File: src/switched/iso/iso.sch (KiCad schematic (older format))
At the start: 54 parts

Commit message: isolation stage rev 1
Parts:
- removed C?: 1n, symbol Device:C_Small
- removed C?: 33n, symbol Device:C_Small
- removed C? (x2): 2n2, symbol Device:C_Small
- removed C?: 47u, symbol Device:C
- removed C?: 100n, symbol Device:C_Small
- removed D? (x3): D, symbol Device:D
- removed IC?: NCP1252A, SOIC127P600X175-8N, symbol NCP1252CDR2G:NCP1252CDR2G
- removed Q?: Q_NMOS_DGS, symbol Device:Q_NMOS_DGS
- removed R?: 4, symbol Device:R_US
- removed R?: 5k571, symbol Device:R_US
- removed R?: 10R 2W, symbol Device:R_US
- removed R?: 24k, symbol Device:R_US
- removed R? (x2): 10k, symbol Device:R_US
- removed R?: 22k, symbol Device:R_US
- removed R?: 2k, symbol Device:R_US
- removed R?: 1k, symbol Device:R_US
- removed R?: 235, symbol Device:R_US
- removed R?: 565, symbol Device:R_US
- removed U?: TL431D, Package_SO:SOIC-8_3.9x4.9mm_P1.27mm, symbol Reference_Voltage:TL431D
- removed U?: OPAMP, symbol pspice:OPAMP
- added C1, C17, C18, C5, C7: 100n, Capacitor_SMD:C_0603_1608Metric_Pad1.08x0.95mm_HandSolder, symbol Device:C_Small
- added C10, C11, C12, C6, C9: 1n, Capacitor_SMD:C_0603_1608Metric_Pad1.08x0.95mm_HandSolder, symbol Device:C_Small
- added C15: 470n, Capacitor_SMD:C_0603_1608Metric_Pad1.08x0.95mm_HandSolder, symbol Device:C_Small
- added C2: 4.7u, Capacitor_THT:CP_Radial_D8.0mm_P3.50mm, symbol Device:C_Small
- added D1, D4, D5: 1N4007W, Diode_SMD:D_SOD-123F, symbol Device:D
- added IC1: NCP1252ADR2G, Package_SO:SOIC-8_3.9x4.9mm_P1.27mm, symbol NCP1252CDR2G:NCP1252CDR2G
- added Q2: TSD5N50MR, Package_TO_SOT_SMD:TO-252-2, symbol Device:Q_NMOS_GDS
- added R1: 1Meg, Resistor_SMD:R_1206_3216Metric_Pad1.30x1.75mm_HandSolder, symbol Device:R_US
- added R12: 10R, Resistor_THT:R_Axial_DIN0207_L6.3mm_D2.5mm_P2.54mm_Vertical, symbol Device:R_US
- added R15, R3: 1k, Resistor_THT:R_Axial_DIN0207_L6.3mm_D2.5mm_P2.54mm_Vertical, symbol Device:R_US
- added R16: 39k, Resistor_SMD:R_0603_1608Metric_Pad0.98x0.95mm_HandSolder, symbol Device:R_US
- added R18: 15k, Resistor_THT:R_Axial_DIN0309_L9.0mm_D3.2mm_P2.54mm_Vertical, symbol Device:R_US
- added R4, R5, R6, R7: 10, Resistor_SMD:R_0603_1608Metric_Pad0.98x0.95mm_HandSolder, symbol Device:R_US
- added RV1: 5k571, Potentiometer_SMD:Potentiometer_Bourns_TC33X_Vertical, symbol Device:R_POT_TRIM_US
- added RV2, RV3: 2.4, Potentiometer_SMD:Potentiometer_Bourns_TC33X_Vertical, symbol Device:R_POT_TRIM_US
- added RV4: 1k, Potentiometer_SMD:Potentiometer_Bourns_TC33X_Vertical, symbol Device:R_POT_TRIM_US
- added U1: NCP5106, Package_SO:SOIC-8_3.9x4.9mm_P1.27mm, symbol custom:NCP5106
- added U3: TL431LP, Package_TO_SOT_THT:TO-92_Inline, symbol Reference_Voltage:TL431LP
- added U4: MC34072, Package_SO:SOIC-8_3.9x4.9mm_P1.27mm, symbol custom:MC34072
- C13: renamed from C?; value 40u -> 330u; footprint (none) -> Capacitor_SMD:CP_Elec_10x14.3; Checked (none) -> yes; Link (none) -> https://lcsc.com/product-detail/New-Arrivals_Ymin-VKME1651J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; Working Voltage (none) -> 63
- C14, C19, C3, C8: renamed from C?; footprint (none) -> Capacitor_SMD:C_0603_1608Metric_Pad1.08x0.95mm_HandSolder; Checked (none) -> yes; Link (none) -> https://lcsc.com/product-detail/Multilayer-Ceramic-Capacito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; Notes (none) -> On PFC; Working Voltage (none) -> 50
- C16: renamed from C?; value 1u -> 470n; footprint (none) -> Capacitor_SMD:C_0603_1608Metric_Pad1.08x0.95mm_HandSolder; Checked (none) -> yes; Link (none) -> https://lcsc.com/product-detail/Multilayer-Ceramic-Capacito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; Notes (none) -> On PFC; Working Voltage (none) -> 25
- C4: renamed from C?; value 55n -> 47n; footprint (none) -> Capacitor_SMD:C_0603_1608Metric_Pad1.08x0.95mm_HandSolder; Checked (none) -> yes; Link (none) -> https://lcsc.com/product-detail/Multilayer-Ceramic-Capacito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; Working Voltage (none) -> 50
- D2, D3: renamed from D?; footprint (none) -> Diode_SMD:D_SOD-123; Checked (none) -> yes; Link (none) -> https://lcsc.com/product-detail/Zener-Diodes_Slkor-SLKORMIC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
- D6, D7: renamed from D?; footprint (none) -> Diode_SMD:D_SMC; Checked (none) -> yes; Link (none) -> https://lcsc.com/product-detail/Diodes-General-Purpose_Shan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
- D8: renamed from D?; footprint (none) -> Diode_SMD:D_SOD-123; Checked (none) -> yes; Link (none) -> https://lcsc.com/product-detail/Zener-Diodes_Shandong-Jingd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
- J1, J3: renamed from J?; footprint (none) -> Connector_Wire:SolderWire-1.5sqmm_1x02_P6mm_D1.7mm_OD3mm
- J2, J4: renamed from J?; footprint (none) -> Connector_PinSocket_2.54mm:PinSocket_1x02_P2.54mm_Vertical
- L1: renamed from L?; value 150u -> 47u; footprint (none) -> custom:TMPC1265HP-470MG-D; Checked (none) -> yes; Link (none) -> https://lcsc.com/product-detail/Power-Inductors_TAI-TECH-TM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
- Q1: renamed from Q?; value Q_NMOS_DGS -> TSD5N50MR; footprint (none) -> Package_TO_SOT_SMD:TO-252-2; symbol Device:Q_NMOS_DGS -> Device:Q_NMOS_GDS; Checked (none) -> yes; Link (none) -> https://lcsc.com/product-detail/New-Arrivals_Truesemi-TSD5N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
- R10, R9: renamed from R?; value 47k -> 39k; footprint (none) -> Resistor_SMD:R_0603_1608Metric_Pad0.98x0.95mm_HandSolder; Checked (none) -> yes; Link (none) -> https://lcsc.com/product-detail/High-Precision-Low-TCR-SMD-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; Notes (none) -> On PFC; Working Voltage (none) -> 75
- R11: renamed from R?; value 10R 2W -> 10R; footprint (none) -> Resistor_THT:R_Axial_DIN0207_L6.3mm_D2.5mm_P2.54mm_Vertical; Checked (none) -> yes; Link (none) -> https://lcsc.com/product-detail/Carbon-Film-Resistors_TyoHM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
- R13, R14: renamed from R?; footprint (none) -> Resistor_THT:R_Axial_DIN0207_L6.3mm_D2.5mm_P2.54mm_Vertical; Checked (none) -> yes; Link (none) -> https://lcsc.com/product-detail/Carbon-Film-Resistors_CCO-C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
- R17: renamed from R?; value 10k -> 39k; footprint (none) -> Resistor_SMD:R_0603_1608Metric_Pad0.98x0.95mm_HandSolder; Checked (none) -> yes; Link (none) -> https://lcsc.com/product-detail/High-Precision-Low-TCR-SMD-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; Notes (none) -> On PFC; Working Voltage (none) -> 75
- R2: renamed from R?; value 2Meg -> 1Meg; footprint (none) -> Resistor_SMD:R_1206_3216Metric_Pad1.30x1.75mm_HandSolder; Checked (none) -> yes; Link (none) -> https://lcsc.com/product-detail/High-Voltage-Resistor_Ever-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; Notes (none) -> On PFC; Working Voltage (none) -> 500
- R8: renamed from R?; value 17k2 -> 16.9k; footprint (none) -> Resistor_SMD:R_0603_1608Metric_Pad0.98x0.95mm_HandSolder; Checked (none) -> yes; Link (none) -> https://lcsc.com/product-detail/High-Precision-Low-TCR-SMD-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
- Rsense1: renamed from Rsense; value 0.6 1W -> 0.51 1W; footprint (none) -> Resistor_SMD:R_2512_6332Metric_Pad1.40x3.35mm_HandSolder; Checked (none) -> yes; Link (none) -> https://lcsc.com/product-detail/Low-Resistors-Current-Sense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
- T1: renamed from T?; footprint (none) -> custom:CSV-E25-13-7-1S-6P-C; Checked (none) -> yes
- U2: renamed from U?; value NSL-32 -> ORPC-817C; footprint OptoDevice:Luna_NSL-32 -> custom:ORPC-817C; Checked (none) -> yes; Link (none) -> https://lcsc.com/product-detail/Optocouplers_Orient-ORPC-81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
- U5: renamed from U?; footprint Package_TO_SOT_SMD:SOT-223-3_TabPin2 -> Package_TO_SOT_THT:TO-220-3_Horizontal_TabDown; Checked (none) -> yes; Link (none) -> https://lcsc.com/product-detail/Dropout-Regulators-LDO_STMi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
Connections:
- net FB: now also C6.1, IC1.1 (FB)
- net cs: now also Q2.3 (S), R3.1
- net gnd: now also J1.2 (Pin_2), J2.2 (Pin_2), C1.2, C2.1, C6.2, C7.2, D5.2 (A), IC1.5 (GND), RV1.2, U1.4 (GND); no longer J1.1 (Pin_1), J2.1 (Pin_1)
- net vfb: now also J4.1 (Pin_1), R16.2; no longer J4.2 (Pin_2)
- net vin: now also J1.1 (Pin_1), Q1.2 (D), D4.1 (K), R1.1; no longer Q1.1 (D), R2.1
- net voutn: now also J3.2 (Pin_2), J4.2 (Pin_2), C15.2, C17.1, C18.2, R12.2, R18.2, RV3.3, RV4.1, U3.2 (A), U4.4 (Vee); no longer J3.1 (Pin_1), J4.1 (Pin_1)
- net voutp: now also J3.1 (Pin_1), C18.1, R18.1, RV3.1, U4.8 (Vcc); no longer J3.2 (Pin_2)
- net at C3.1, R2.2: now also IC1.2 (BO), RV1.3
- net at C4.2: now also IC1.3 (CS), R3.2
- net at R8.1: now also IC1.4 (RT)
- net at D2.1 (K), R9.1: now also Q1.1 (G), R5.2; no longer Q1.2 (G)
- net at D2.2 (A), Q1.3 (S), R9.2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: now also D5.1 (K), R6.1
- net at T1.2 (AB): now also D4.2 (A), Q2.2 (D)
- net at D3.1 (K), R10.1: now also Q2.1 (G), R7.2
- net at D6.1 (K), D7.1 (K), L1.2: now also C10.1, C11.2, C12.2, C9.1
- net at R11.1: now also C10.2, C9.2
- net at C14.1, R14.2, U2.2 (K): now also U3.3 (K)
- net at C14.2: now also R15.2, U3.1 (REF)
- net at C16.1, R13.1, U5.2 (VO): now also C15.1, RV4.3
- net at D8.1 (K): now also C17.2, R16.1, U4.5 (Pos2)
- net at U5.1 (ADJ): now also RV4.2
- net v12 renamed vcc
- net vcc: now also J2.1 (Pin_1), C1.1, C2.2, D1.2 (A), IC1.7 (VCC), U1.1 (VCC); no longer J2.2 (Pin_2)
- new net: C7.1, IC1.8 (SS)
- new net: R1.2, R2.1
- new net: R15.1, RV2.1, U4.1 (Out1)
- new net: RV2.2, U4.2 (Neg1)
- new net: RV3.2, U4.3 (Pos1)
- new net: C11.1, C12.1, R12.1
- new net: C5.1, R4.1, U1.8 (VBOOT)
- new net: D1.1 (K), R4.2
- new net: R5.1, U1.7 (DRV_HI)
- new net: R7.1, U1.5 (DRV_LO)
- new net: C5.2, R6.2, U1.6 (BRIDGE)
- new net DRV: IC1.6 (DRV), U1.2 (IN_HI), U1.3 (IN_LO)
- new net buf_fb: RV2.3, U4.6 (Neg2), U4.7 (Out2)
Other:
- moved on the sheet: C13, C14, C16, C19, C3, C4, C8, D2, D3, D6, D7, D8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

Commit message: Midterm report
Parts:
- C1, C14, C17, C18, C19, C5, C7, C8: Price (none) -> 0.0032
- C10, C11, C12, C3, C6, C9, R14, R15, R3: Price (none) -> 0.0031
- C13: Price (none) -> 0.1728
- C15, C16: Price (none) -> 0.0112
- C2: Price (none) -> 0.039
- C4: Price (none) -> 0.0036
- D1, D4, D5: Price (none) -> 0.0067
- D2, D3: Price (none) -> 0.0123
- D6, D7: Price (none) -> 0.0718
- D8: Price (none) -> 0.0173
- IC1: Price (none) -> 0.5338
- L1: Price (none) -> 0.6745
- Q1, Q2: Price (none) -> 0.1438
- R1, R2: Price (none) -> 0.0234
- R10, R16, R17, R18, R9: Price (none) -> 0.0071
- R11, R12: Price (none) -> 0.0081
- R13: Price (none) -> 0.0052
- R4, R5, R6, R7: Price (none) -> 0.0012
- R8: Price (none) -> 0.008
- RV1: Price (none) -> 0.0538
- RV2, RV3: Price (none) -> 0.055
- RV4: Price (none) -> 0.0536
- Rsense1: Price (none) -> 0.051
- T1: Price (none) -> 1.337
- U1: Price (none) -> 0.6077
- U2: Price (none) -> 0.0381
- U3: Price (none) -> 0.0228
- U4: Price (none) -> 0.1754
- U5: Price (none) -> 0.2599
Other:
- moved on the sheet: C1, C10, C11, C12, C13, C14, C15, C16, C17, C18, C19, C2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

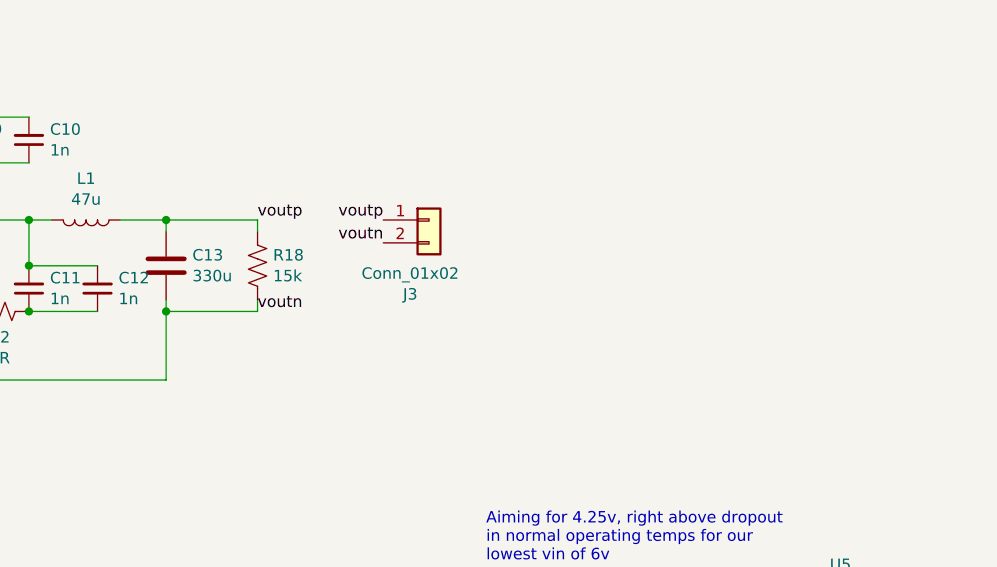
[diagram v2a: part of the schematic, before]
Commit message: Iso output changed to ceramic caps
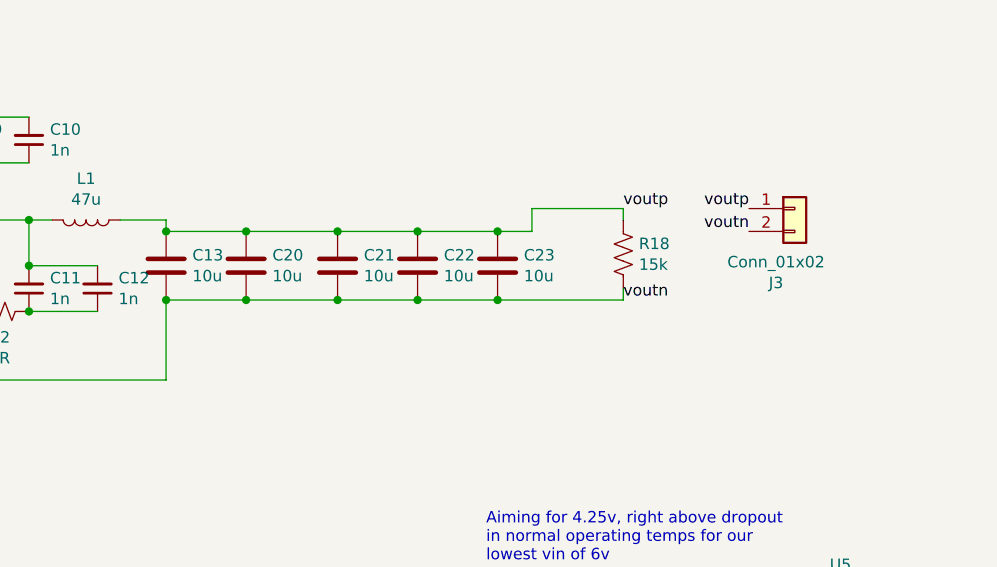
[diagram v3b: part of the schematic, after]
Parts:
- added C20, C21, C22, C23: 10u, Capacitor_SMD:C_1206_3216Metric_Pad1.33x1.80mm_HandSolder, symbol Device:C
- C13: value 330u -> 10u; footprint Capacitor_SMD:CP_Elec_10x14.3 -> Capacitor_SMD:C_1206_3216Metric_Pad1.33x1.80mm_HandSolder; Checked yes -> (none); Link https://lcsc.com/product-detail/New-Arrivals_Ymin-VKME1651J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 -> https://lcsc.com/product-detail/Multilayer-Ceramic-Capacito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; Notes (none) -> On linear; Price 0.1728 -> (none); Working Voltage 63 -> (none)
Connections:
- net voutn: now also C20.2, C21.2, C22.2, C23.2
- net voutp: now also C20.1, C21.1, C22.1, C23.1
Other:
- moved on the sheet: J3, R18
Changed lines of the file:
@@
 	0    1    1    0
 $EndComp
-$Comp
-L Device:C C13
-U 1 1 60350F8F
-P 5600 2300
-F 0 "C13" H 5715 2346 50  0000 L CNN
-F 1 "330u" H 5715 2255 50  0000 L CNN
-F 2 "Capacitor_SMD:CP_Elec_10x14.3" H 5638 2150 50  0001 C CNN
-F 3 "VKME1651J331MV" H 5600 2300 50  0001 C CNN
-F 4 "https://lcsc.com/product-detail/New-Arrivals_Ymin-VKME1651J331MV_C487393.html" H 5600 2300 50  0001 C CNN "Link"
-F 5 "yes" H 5600 2300 50  0001 C CNN "Checked"
-F 6 "63" H 5600 2300 50  0001 C CNN "Working Voltage"
-F 7 "0.1728" H 5600 2300 50  0001 C CNN "Price"
-	1    5600 2300
-	1    0    0    -1
-$EndComp
-Text Label 6000 2100 0    50   ~ 0
+Text Label 7600 2050 0    50   ~ 0
 voutp
-Text Label 6000 2500 0    50   ~ 0
+Text Label 7600 2450 0    50   ~ 0
 voutn
 $Comp
 L Connector_Generic:Conn_01x02 J3
 U 1 1 6035B66C
-P 6750 2100
-F 0 "J3" H 6668 1775 50  0000 C CNN
-F 1 "Conn_01x02" H 6668 1866 50  0000 C CNN
-F 2 "Connector_Wire:SolderWire-1.5sqmm_1x02_P6mm_D1.7mm_OD3mm" H 6750 2100 50  0001 C CNN
-F 3 "~" H 6750 2100 50  0001 C CNN
-	1    6750 2100
-	1    0    0    -1
-$EndComp
-Text Label 6550 2200 2    50   ~ 0
+P 8350 2050
+F 0 "J3" H 8268 1725 50  0000 C CNN
+F 1 "Conn_01x02" H 8268 1816 50  0000 C CNN
+F 2 "Connector_Wire:SolderWire-1.5sqmm_1x02_P6mm_D1.7mm_OD3mm" H 8350 2050 50  0001 C CNN
+F 3 "~" H 8350 2050 50  0001 C CNN
+	1    8350 2050
+	1    0    0    -1
+$EndComp
+Text Label 8150 2150 2    50   ~ 0
 voutn
-Text Label 6550 2100 2    50   ~ 0
+Text Label 8150 2050 2    50   ~ 0
 voutp
 Text Label 3650 6050 2    50   ~ 0
@@
 	5400 2100 5600 2100
 Wire Wire Line
-	5600 2450 5600 2500
-Wire Wire Line
-	6000 2500 5600 2500
-Connection ~ 5600 2500
-Wire Wire Line
-	5600 2500 5600 2800
-Wire Wire Line
 	5600 2150 5600 2100
-Connection ~ 5600 2100
-Wire Wire Line
-	5600 2100 6000 2100
+Wire Wire Line
+	7200 2050 7600 2050
 Wire Wire Line
 	5000 2300 5300 2300
@@
 L Device:R_US R18
 U 1 1 605850DD
-P 6000 2300
-F 0 "R18" H 6068 2346 50  0000 L CNN
-F 1 "15k" H 6068 2255 50  0000 L CNN
-F 2 "Resistor_THT:R_Axial_DIN0309_L9.0mm_D3.2mm_P2.54mm_Vertical" V 6040 2290 50  0001 C CNN
-F 3 "MO1/2W-15K±5%-XT52" H 6000 2300 50  0001 C CNN
-F 4 "https://lcsc.com/product-detail/Metal-Oxide-Resistors_FlyWin-MO1-2W-15K-5-XT52_C601770.html" H 6000 2300 50  0001 C CNN "Link"
-F 5 "yes" H 6000 2300 50  0001 C CNN "Checked"
-F 6 "0.0071" H 6000 2300 50  0001 C CNN "Price"
-	1    6000 2300
-	1    0    0    -1
-$EndComp
-Wire Wire Line
-	6000 2150 6000 2100
-Wire Wire Line
-	6000 2450 6000 2500
+P 7600 2250
+F 0 "R18" H 7668 2296 50  0000 L CNN
+F 1 "15k" H 7668 2205 50  0000 L CNN
+F 2 "Resistor_THT:R_Axial_DIN0309_L9.0mm_D3.2mm_P2.54mm_Vertical" V 7640 2240 50  0001 C CNN
+F 3 "MO1/2W-15K±5%-XT52" H 7600 2250 50  0001 C CNN
+F 4 "https://lcsc.com/product-detail/Metal-Oxide-Resistors_FlyWin-MO1-2W-15K-5-XT52_C601770.html" H 7600 2250 50  0001 C CNN "Link"
+F 5 "yes" H 7600 2250 50  0001 C CNN "Checked"
+F 6 "0.0071" H 7600 2250 50  0001 C CNN "Price"
+	1    7600 2250
+	1    0    0    -1
+$EndComp
+Wire Wire Line
+	7600 2100 7600 2050
+Wire Wire Line
+	7600 2400 7600 2450
 $Comp
 L Reference_Voltage:TL431LP U3
@@
 Wire Wire Line
 	1800 5650 1850 5650
+$Comp
+L Device:C C13
+U 1 1 6048E788
+P 5600 2300
+F 0 "C13" H 5715 2346 50  0000 L CNN
+F 1 "10u" H 5715 2255 50  0000 L CNN
+F 2 "Capacitor_SMD:C_1206_3216Metric_Pad1.33x1.80mm_HandSolder" H 5638 2150 50  0001 C CNN
+F 3 "C1206X5R106K500NT" H 5600 2300 50  0001 C CNN
+F 4 "https://lcsc.com/product-detail/Multilayer-Ceramic-Capacitors-MLCC-SMD-SMT_SANYEAR-C1206X5R106K500NT_C466808.html" H 5600 2300 50  0001 C CNN "Link"
+F 5 "" H 5600 2300 50  0001 C CNN "Checked"
+F 6 "" H 5600 2300 50  0001 C CNN "Working Voltage"
+F 7 "" H 5600 2300 50  0001 C CNN "Price"
+F 8 "On linear" H 5600 2300 50  0001 C CNN "Notes"
+	1    5600 2300
+	1    0    0    -1
+$EndComp
+Wire Wire Line
+	5600 2450 5600 2800
+$Comp
+L Device:C C20
+U 1 1 604B2B40
+P 5950 2300
+F 0 "C20" H 6065 2346 50  0000 L CNN
+F 1 "10u" H 6065 2255 50  0000 L CNN
+F 2 "Capacitor_SMD:C_1206_3216Metric_Pad1.33x1.80mm_HandSolder" H 5988 2150 50  0001 C CNN
+F 3 "C1206X5R106K500NT" H 5950 2300 50  0001 C CNN
+F 4 "https://lcsc.com/product-detail/Multilayer-Ceramic-Capacitors-MLCC-SMD-SMT_SANYEAR-C1206X5R106K500NT_C466808.html" H 5950 2300 50  0001 C CNN "Link"
+F 5 "" H 5950 2300 50  0001 C CNN "Checked"
+F 6 "" H 5950 2300 50  0001 C CNN "Working Voltage"
+F 7 "" H 5950 2300 50  0001 C CNN "Price"
+F 8 "On linear" H 5950 2300 50  0001 C CNN "Notes"
+	1    5950 2300
+	1    0    0    -1
+$EndComp
+$Comp
+L Device:C C21
+U 1 1 604B3526
+P 6350 2300
+F 0 "C21" H 6465 2346 50  0000 L CNN
+F 1 "10u" H 6465 2255 50  0000 L CNN
+F 2 "Capacitor_SMD:C_1206_3216Metric_Pad1.33x1.80mm_HandSolder" H 6388 2150 50  0001 C CNN
+F 3 "C1206X5R106K500NT" H 6350 2300 50  0001 C CNN
+F 4 "https://lcsc.com/product-detail/Multilayer-Ceramic-Capacitors-MLCC-SMD-SMT_SANYEAR-C1206X5R106K500NT_C466808.html" H 6350 2300 50  0001 C CNN "Link"
+F 5 "" H 6350 2300 50  0001 C CNN "Checked"
+F 6 "" H 6350 2300 50  0001 C CNN "Working Voltage"
+F 7 "" H 6350 2300 50  0001 C CNN "Price"
+F 8 "On linear" H 6350 2300 50  0001 C CNN "Notes"
+	1    6350 2300
+	1    0    0    -1
+$EndComp
+$Comp
+L Device:C C22
+U 1 1 604B3F28
+P 6700 2300
+F 0 "C22" H 6815 2346 50  0000 L CNN
+F 1 "10u" H 6815 2255 50  0000 L CNN
+F 2 "Capacitor_SMD:C_1206_3216Metric_Pad1.33x1.80mm_HandSolder" H 6738 2150 50  0001 C CNN
+F 3 "C1206X5R106K500NT" H 6700 2300 50  0001 C CNN
+F 4 "https://lcsc.com/product-detail/Multilayer-Ceramic-Capacitors-MLCC-SMD-SMT_SANYEAR-C1206X5R106K500NT_C466808.html" H 6700 2300 50  0001 C CNN "Link"
+F 5 "" H 6700 2300 50  0001 C CNN "Checked"
+F 6 "" H 6700 2300 50  0001 C CNN "Working Voltage"
+F 7 "" H 6700 2300 50  0001 C CNN "Price"
+F 8 "On linear" H 6700 2300 50  0001 C CNN "Notes"
+	1    6700 2300
+	1    0    0    -1
+$EndComp
+$Comp
+L Device:C C23
+U 1 1 604B4A4B
+P 7050 2300
+F 0 "C23" H 7165 2346 50  0000 L CNN
+F 1 "10u" H 7165 2255 50  0000 L CNN
+F 2 "Capacitor_SMD:C_1206_3216Metric_Pad1.33x1.80mm_HandSolder" H 7088 2150 50  0001 C CNN
+F 3 "C1206X5R106K500NT" H 7050 2300 50  0001 C CNN
+F 4 "https://lcsc.com/product-detail/Multilayer-Ceramic-Capacitors-MLCC-SMD-SMT_SANYEAR-C1206X5R106K500NT_C466808.html" H 7050 2300 50  0001 C CNN "Link"
+F 5 "" H 7050 2300 50  0001 C CNN "Checked"
+F 6 "" H 7050 2300 50  0001 C CNN "Working Voltage"
+F 7 "" H 7050 2300 50  0001 C CNN "Price"
+F 8 "On linear" H 7050 2300 50  0001 C CNN "Notes"
+	1    7050 2300
+	1    0    0    -1
+$EndComp
+Wire Wire Line
+	5600 2450 5950 2450
+Connection ~ 5600 2450
+Connection ~ 5950 2450
+Wire Wire Line
+	5950 2450 6350 2450
+Connection ~ 6350 2450
+Wire Wire Line
+	6350 2450 6700 2450
+Connection ~ 6700 2450
+Wire Wire Line
+	6700 2450 7050 2450
+Connection ~ 7050 2450
+Wire Wire Line
+	7050 2450 7600 2450
+Wire Wire Line
+	5600 2150 5950 2150
+Wire Wire Line
+	7200 2150 7200 2050
+Connection ~ 5600 2150
+Connection ~ 5950 2150
+Wire Wire Line
+	5950 2150 6350 2150
+Connection ~ 6350 2150
+Wire Wire Line
+	6350 2150 6700 2150
+Connection ~ 6700 2150
+Wire Wire Line
+	6700 2150 7050 2150
+Connection ~ 7050 2150
+Wire Wire Line
+	7050 2150 7200 2150
 $EndSCHEMATC
